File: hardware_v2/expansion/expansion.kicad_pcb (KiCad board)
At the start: 2 copper layers, 50 x 59 mm, 13 parts, among them J2 Conn_02x10_Odd_Even

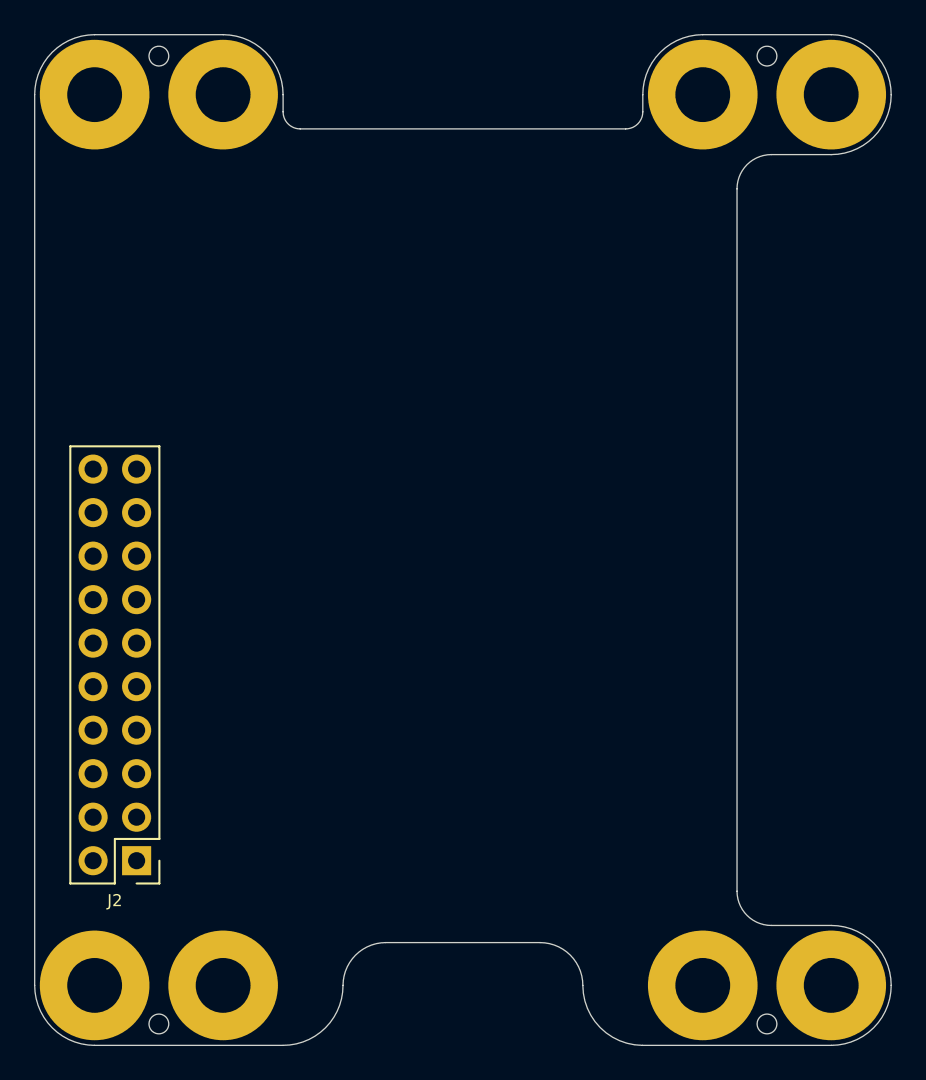
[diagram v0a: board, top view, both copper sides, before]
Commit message: Expansion PCB: Add 4-layer stackup and ground planes
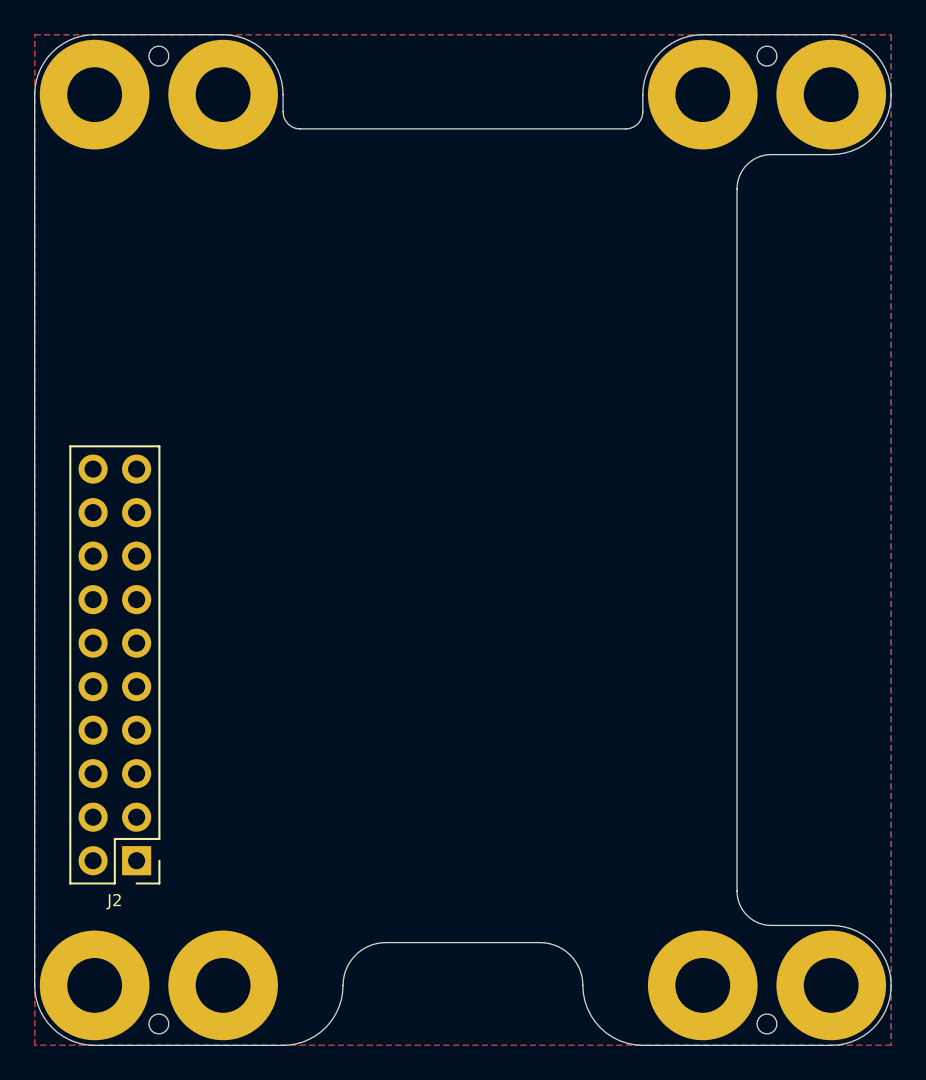
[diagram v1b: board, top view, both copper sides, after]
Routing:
- added copper zone on B.Cu, net GND
- added copper zone on F.Cu, net GND
- added copper zone on In1.Cu, net GND
- added copper zone on In2.Cu, net GND
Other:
- copper layers 2 -> 4
- rule pad_to_mask_clearance: 0 -> 0.038
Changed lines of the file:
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@@
 (kicad_pcb (version 20221018) (generator pcbnew)
   (general
-    (thickness 1.6)
+    (thickness 1.61668)
   )
   (paper "A4")
   (layers
     (0 "F.Cu" signal)
+    (1 "In1.Cu" signal)
+    (2 "In2.Cu" signal)
     (31 "B.Cu" signal)
     (32 "B.Adhes" user "B.Adhesive")
@@
   )
   (setup
-    (pad_to_mask_clearance 0)
+    (stackup
+      (layer "F.SilkS" (type "Top Silk Screen") (color "White"))
+      (layer "F.Paste" (type "Top Solder Paste"))
+      (layer "F.Mask" (type "Top Solder Mask") (color "Green") (thickness 0.01524))
+      (layer "F.Cu" (type "copper") (thickness 0.035))
+      (layer "dielectric 1" (type "prepreg") (color "FR4 natural") (thickness 0.2104) (material "FR4") (epsilon_r 4.4) (loss_tangent 0.02))
+      (layer "In1.Cu" (type "copper") (thickness 0.0152))
+      (layer "dielectric 2" (type "core") (color "FR4 natural") (thickness 1.065) (material "FR4") (epsilon_r 4.6) (loss_tangent 0.02))
+      (layer "In2.Cu" (type "copper") (thickness 0.0152))
+      (layer "dielectric 3" (type "prepreg") (color "FR4 natural") (thickness 0.2104) (material "FR4") (epsilon_r 4.4) (loss_tangent 0.02))
+      (layer "B.Cu" (type "copper") (thickness 0.035))
+      (layer "B.Mask" (type "Bottom Solder Mask") (color "Green") (thickness 0.01524))
+      (layer "B.Paste" (type "Bottom Solder Paste"))
+      (layer "B.SilkS" (type "Bottom Silk Screen") (color "White"))
+      (copper_finish "None")
+      (dielectric_constraints no)
+    )
+    (pad_to_mask_clearance 0.038)
+    (allow_soldermask_bridges_in_footprints yes)
     (grid_origin 125 60)
     (pcbplotparams
@@
   (gr_arc (start 135.5 61) (mid 136.525126 58.525126) (end 139 57.5)
     (stroke (width 0.05) (type default)) (layer "Edge.Cuts"))
+  (zone (net 1) (net_name "GND") (layers "F.Cu" "In1.Cu" "In2.Cu" "B.Cu") (name "Ground plane") (hatch edge 0.5)
+    (connect_pads (clearance 0.3))
+    (min_thickness 0.2) (filled_areas_thickness no)
+    (fill yes (thermal_gap 0.25) (thermal_bridge_width 0.25))
+    (polygon
+      (pts
+        (xy 100 57.5)
+        (xy 150 57.5)
+        (xy 150 116.5)
+        (xy 100 116.5)
+      )
+    )
+  )
 )
